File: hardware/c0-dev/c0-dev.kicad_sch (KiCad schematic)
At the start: 16 parts, among them J101 2913730000, J102 2913710000, J103 2913730000, J104 2913730000, J105 2913730000, J106 2913710000, J107 2913730000, J108 2913730000, J109 2913730000, J111 2913730000, J112 2913730000, J113 2913730000, J114 2913730000

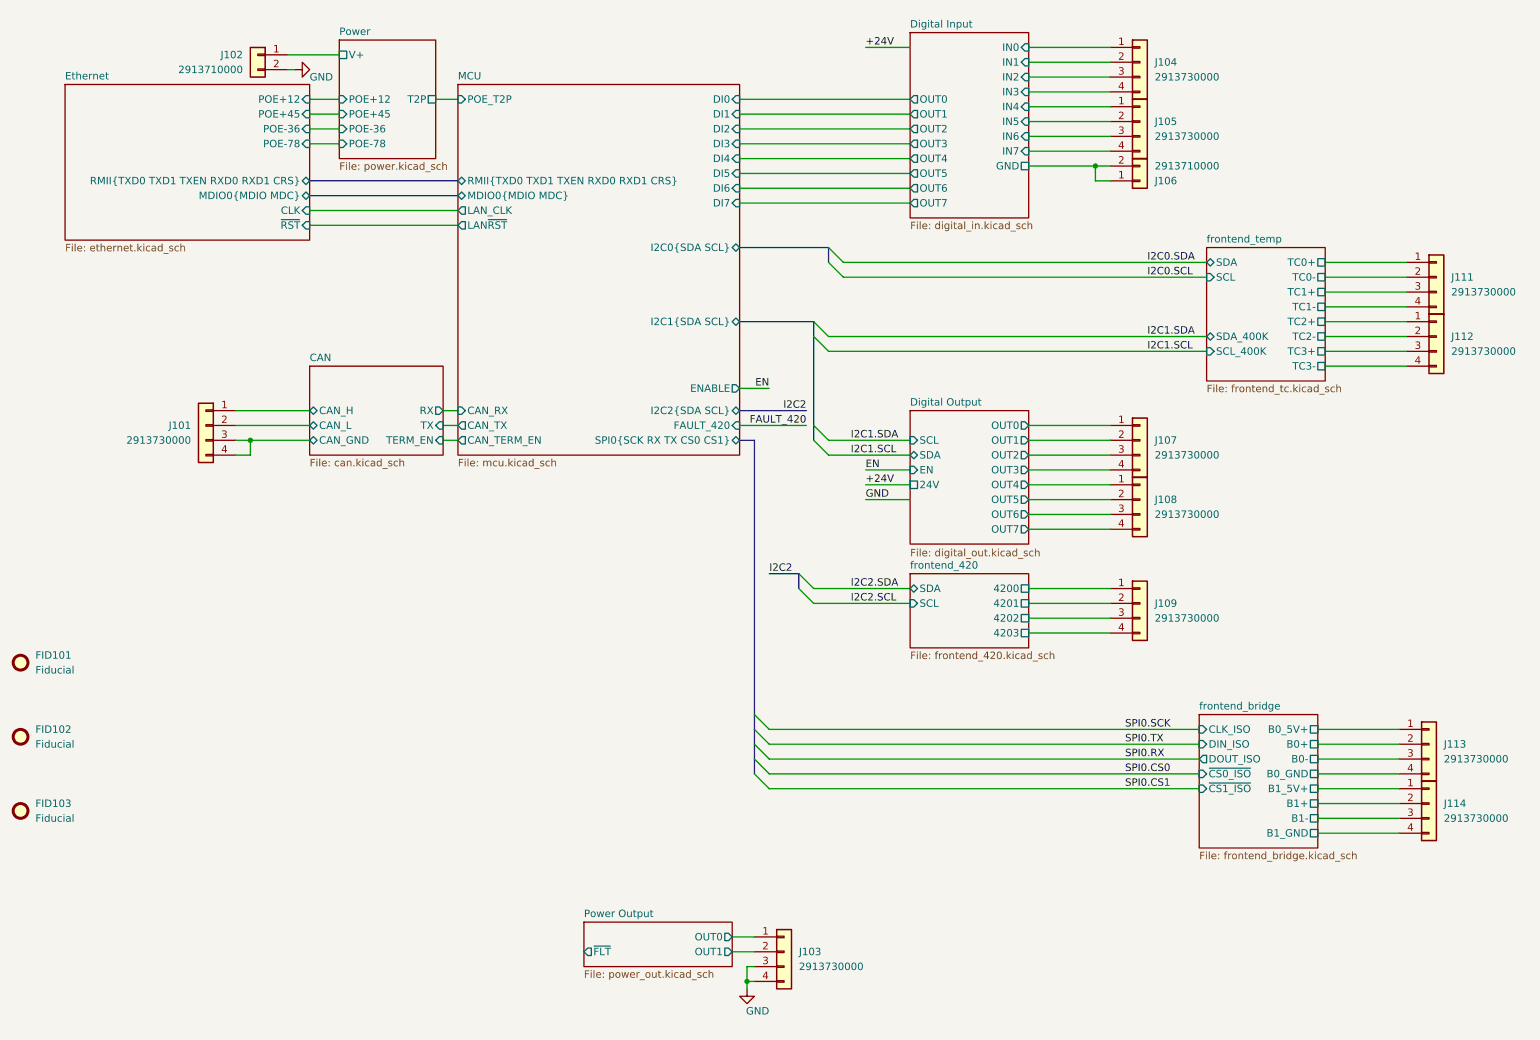
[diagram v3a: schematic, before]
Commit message: added LEDs
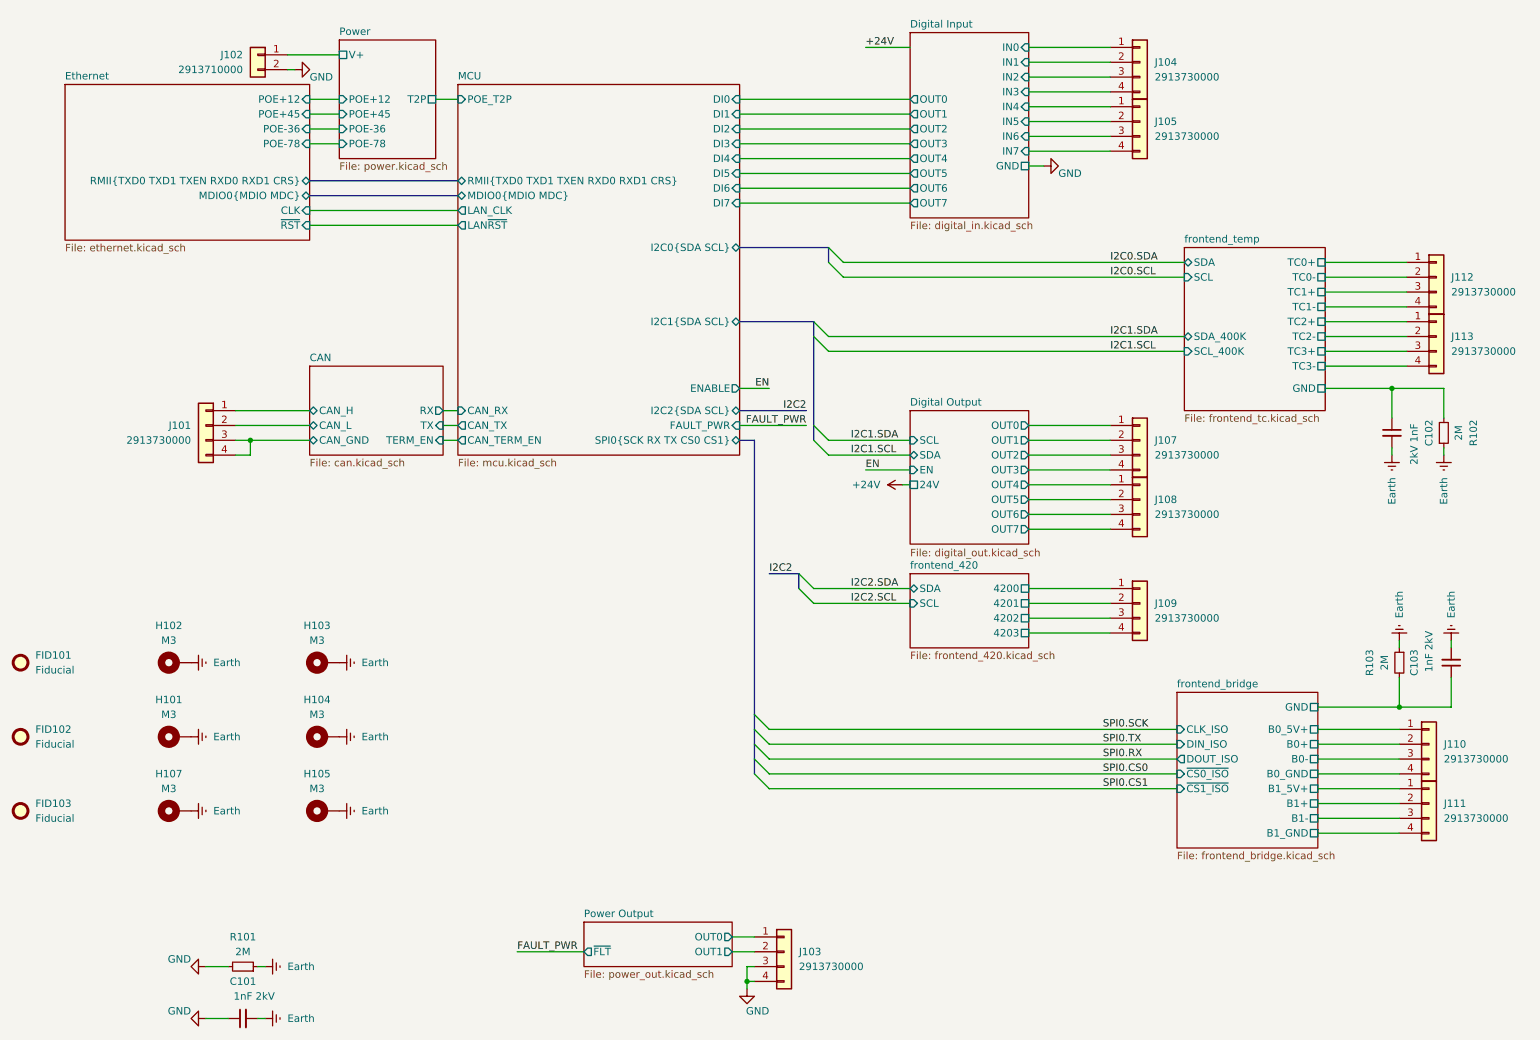
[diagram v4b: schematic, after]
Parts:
- removed J106: 2913710000, conduit:2913710000, symbol Connector_Generic:Conn_01x02
- added C101, C102, C103: 1nF, Capacitor_SMD:C_1206_3216Metric, symbol Device:C_Small
- added H101, H102, H103, H104, H105, H107: M3, MountingHole:MountingHole_3.5mm_Pad_TopBottom, symbol Mechanical:MountingHole_Pad
- added R101, R102, R103: 2M, Resistor_SMD:R_1206_3216Metric, symbol Device:R_Small
- renumbered J113 to J110, J114 to J111, J111 to J112, J112 to J113
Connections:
- net GND: now also C101.1, R101.2
- new net Earth: C101.2, C102.2, C103.2, H101.1, H102.1, H103.1, H104.1, H105.1, H107.1, R101.1, R102.1, R103.1
- new net frontend_bridge/GND: C103.1, R103.2
- new net frontend_temp/GND: C102.1, R102.2
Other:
- sheet MCU ports: added FAULT_PWR; removed FAULT_420
- sheet frontend_bridge ports: added GND; removed none
- sheet frontend_temp ports: added GND; removed none

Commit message: rgb's and 70x160mm
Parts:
- renumbered H102 to H101, H101 to H102, H107 to H103, H103 to H104, H104 to H105, H105 to H106, J107 to J106, J108 to J107, J109 to J108, J110 to J109, J111 to J110, J112 to J111, J113 to J112, R103 to R102, R102 to R103
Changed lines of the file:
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@@
 		(dnp no)
 		(fields_autoplaced yes)
-		(property "Reference" "H102"
+		(property "Reference" "H101"
 			(at 50.8 120.65 90)
 			(show_name no)
@@
 			(project "c0-dev"
 				(path "/b8347a0e-ad04-4414-969d-3c64a611d74e"
-					(reference "H102")
+					(reference "H101")
 					(unit 1)
 				)
@@
 		(dnp no)
 		(fields_autoplaced yes)
-		(property "Reference" "#PWR0109"
+		(property "Reference" "#PWR0117"
 			(at 269.24 97.79 0)
 			(hide yes)
@@
 			(project "c0-dev"
 				(path "/b8347a0e-ad04-4414-969d-3c64a611d74e"
-					(reference "#PWR0109")
+					(reference "#PWR0117")
 					(unit 1)
 				)
@@
 		(dnp no)
 		(fields_autoplaced yes)
-		(property "Reference" "#PWR0113"
+		(property "Reference" "#PWR0103"
 			(at 60.96 152.4 0)
 			(hide yes)
@@
 			(project "c0-dev"
 				(path "/b8347a0e-ad04-4414-969d-3c64a611d74e"
-					(reference "#PWR0113")
+					(reference "#PWR0103")
 					(unit 1)
 				)
@@
 		(dnp no)
 		(fields_autoplaced yes)
-		(property "Reference" "#PWR0115"
+		(property "Reference" "#PWR0101"
 			(at 60.96 127 0)
 			(hide yes)
@@
 			(project "c0-dev"
 				(path "/b8347a0e-ad04-4414-969d-3c64a611d74e"
-					(reference "#PWR0115")
+					(reference "#PWR0101")
 					(unit 1)
 				)
@@
 		(in_pos_files yes)
 		(dnp no)
-		(property "Reference" "R103"
+		(property "Reference" "R102"
 			(at 256.54 127 90)
 			(show_name no)
@@
 			(project "c0-dev"
 				(path "/b8347a0e-ad04-4414-969d-3c64a611d74e"
-					(reference "R103")
+					(reference "R102")
 					(unit 1)
 				)
@@
 		(dnp no)
 		(fields_autoplaced yes)
-		(property "Reference" "H101"
+		(property "Reference" "H102"
 			(at 50.8 133.35 90)
 			(show_name no)
@@
 			(project "c0-dev"
 				(path "/b8347a0e-ad04-4414-969d-3c64a611d74e"
-					(reference "H101")
+					(reference "H102")
 					(unit 1)
 				)
@@
 		(in_pos_files yes)
 		(dnp no)
-		(property "Reference" "R102"
+		(property "Reference" "R103"
 			(at 274.32 87.63 90)
 			(show_name no)
@@
 			(project "c0-dev"
 				(path "/b8347a0e-ad04-4414-969d-3c64a611d74e"
-					(reference "R102")
+					(reference "R103")
 					(unit 1)
 				)
@@
 		(dnp no)
 		(fields_autoplaced yes)
-		(property "Reference" "#PWR0108"
+		(property "Reference" "#PWR0113"
 			(at 180.34 96.52 0)
 			(hide yes)
@@
 			(project "c0-dev"
 				(path "/b8347a0e-ad04-4414-969d-3c64a611d74e"
-					(reference "#PWR0108")
+					(reference "#PWR0113")
 					(unit 1)
 				)
@@
 		(dnp no)
 		(fields_autoplaced yes)
-		(property "Reference" "#PWR0116"
+		(property "Reference" "#PWR0109"
 			(at 86.36 127 0)
 			(hide yes)
@@
 			(project "c0-dev"
 				(path "/b8347a0e-ad04-4414-969d-3c64a611d74e"
-					(reference "#PWR0116")
+					(reference "#PWR0109")
 					(unit 1)
 				)
@@
 		(dnp no)
 		(fields_autoplaced yes)
-		(property "Reference" "H105"
+		(property "Reference" "H106"
 			(at 76.2 146.05 90)
 			(show_name no)
@@
 			(project "c0-dev"
 				(path "/b8347a0e-ad04-4414-969d-3c64a611d74e"
-					(reference "H105")
+					(reference "H106")
 					(unit 1)
 				)
@@
 		(dnp no)
 		(fields_autoplaced yes)
-		(property "Reference" "J111"
+		(property "Reference" "J110"
 			(at 269.24 151.1299 0)
 			(show_name no)
@@
 			(project "c0-dev"
 				(path "/b8347a0e-ad04-4414-969d-3c64a611d74e"
-					(reference "J111")
+					(reference "J110")
 					(unit 1)
 				)
@@
 		(in_pos_files yes)
 		(dnp no)
-		(property "Reference" "#PWR0106"
+		(property "Reference" "#PWR0104"
 			(at 50.8 179.07 0)
 			(hide yes)
@@
 			(project "c0-dev"
 				(path "/b8347a0e-ad04-4414-969d-3c64a611d74e"
-					(reference "#PWR0106")
+					(reference "#PWR0104")
 					(unit 1)
 				)
@@
 		(dnp no)
 		(fields_autoplaced yes)
-		(property "Reference" "#PWR0114"
+		(property "Reference" "#PWR0102"
 			(at 60.96 139.7 0)
 			(hide yes)
@@
 			(project "c0-dev"
 				(path "/b8347a0e-ad04-4414-969d-3c64a611d74e"
-					(reference "#PWR0114")
+					(reference "#PWR0102")
 					(unit 1)
 				)
@@
 		(dnp no)
 		(fields_autoplaced yes)
-		(property "Reference" "J110"
+		(property "Reference" "J109"
 			(at 269.24 140.9699 0)
 			(show_name no)
@@
 			(project "c0-dev"
 				(path "/b8347a0e-ad04-4414-969d-3c64a611d74e"
-					(reference "J110")
+					(reference "J109")
 					(unit 1)
 				)
@@
 		(dnp no)
 		(fields_autoplaced yes)
-		(property "Reference" "H104"
+		(property "Reference" "H105"
 			(at 76.2 133.35 90)
 			(show_name no)
@@
 			(project "c0-dev"
 				(path "/b8347a0e-ad04-4414-969d-3c64a611d74e"
-					(reference "H104")
+					(reference "H105")
 					(unit 1)
 				)
@@
 		(dnp no)
 		(fields_autoplaced yes)
-		(property "Reference" "J109"
+		(property "Reference" "J108"
 			(at 219.71 116.8399 0)
 			(show_name no)
@@
 			(project "c0-dev"
 				(path "/b8347a0e-ad04-4414-969d-3c64a611d74e"
-					(reference "J109")
+					(reference "J108")
 					(unit 1)
 				)
@@
 		(dnp no)
 		(fields_autoplaced yes)
-		(property "Reference" "#PWR0118"
+		(property "Reference" "#PWR0111"
 			(at 86.36 152.4 0)
 			(hide yes)
@@
 			(project "c0-dev"
 				(path "/b8347a0e-ad04-4414-969d-3c64a611d74e"
-					(reference "#PWR0118")
+					(reference "#PWR0111")
 					(unit 1)
 				)
@@
 		(dnp no)
 		(fields_autoplaced yes)
-		(property "Reference" "#PWR0117"
+		(property "Reference" "#PWR0110"
 			(at 86.36 139.7 0)
 			(hide yes)
@@
 			(project "c0-dev"
 				(path "/b8347a0e-ad04-4414-969d-3c64a611d74e"
-					(reference "#PWR0117")
+					(reference "#PWR0110")
 					(unit 1)
 				)
@@
 		(dnp no)
 		(fields_autoplaced yes)
-		(property "Reference" "J112"
+		(property "Reference" "J111"
 			(at 270.51 60.9599 0)
 			(show_name no)
@@
 			(project "c0-dev"
 				(path "/b8347a0e-ad04-4414-969d-3c64a611d74e"
-					(reference "J112")
+					(reference "J111")
 					(unit 1)
 				)
@@
 		(dnp no)
 		(fields_autoplaced yes)
-		(property "Reference" "#PWR0111"
+		(property "Reference" "#PWR0118"
 			(at 270.51 116.84 0)
 			(hide yes)
@@
 			(project "c0-dev"
 				(path "/b8347a0e-ad04-4414-969d-3c64a611d74e"
-					(reference "#PWR0111")
+					(reference "#PWR0118")
 					(unit 1)
 				)
@@
 		(in_pos_files yes)
 		(dnp no)
-		(property "Reference" "#PWR0103"
+		(property "Reference" "#PWR0114"
 			(at 207.01 41.91 0)
 			(hide yes)
@@
 			(project "c0-dev"
 				(path "/b8347a0e-ad04-4414-969d-3c64a611d74e"
-					(reference "#PWR0103")
+					(reference "#PWR0114")
 					(unit 1)
 				)
@@
 		(dnp no)
 		(fields_autoplaced yes)
-		(property "Reference" "#PWR0105"
+		(property "Reference" "#PWR0107"
 			(at 73.66 187.96 0)
 			(hide yes)
@@
 			(project "c0-dev"
 				(path "/b8347a0e-ad04-4414-969d-3c64a611d74e"
-					(reference "#PWR0105")
+					(reference "#PWR0107")
 					(unit 1)
 				)
@@
 		(dnp no)
 		(fields_autoplaced yes)
-		(property "Reference" "H103"
+		(property "Reference" "H104"
 			(at 76.2 120.65 90)
 			(show_name no)
@@
 			(project "c0-dev"
 				(path "/b8347a0e-ad04-4414-969d-3c64a611d74e"
-					(reference "H103")
+					(reference "H104")
 					(unit 1)
 				)
@@
 		(dnp no)
 		(fields_autoplaced yes)
-		(property "Reference" "#PWR0110"
+		(property "Reference" "#PWR0115"
 			(at 260.35 97.79 0)
 			(hide yes)
@@
 			(project "c0-dev"
 				(path "/b8347a0e-ad04-4414-969d-3c64a611d74e"
-					(reference "#PWR0110")
+					(reference "#PWR0115")
 					(unit 1)
 				)
@@
 		(in_pos_files yes)
 		(dnp no)
-		(property "Reference" "#PWR0102"
+		(property "Reference" "#PWR0112"
 			(at 149.86 189.23 0)
 			(hide yes)
@@
 			(project "c0-dev"
 				(path "/b8347a0e-ad04-4414-969d-3c64a611d74e"
-					(reference "#PWR0102")
+					(reference "#PWR0112")
 					(unit 1)
 				)
@@
 		(dnp no)
 		(fields_autoplaced yes)
-		(property "Reference" "H107"
+		(property "Reference" "H103"
 			(at 50.8 146.05 90)
 			(show_name no)
@@
 			(project "c0-dev"
 				(path "/b8347a0e-ad04-4414-969d-3c64a611d74e"
-					(reference "H107")
+					(reference "H103")
 					(unit 1)
 				)
@@
 		(in_pos_files yes)
 		(dnp no)
-		(property "Reference" "#PWR0101"
+		(property "Reference" "#PWR0108"
 			(at 78.74 25.4 0)
 			(hide yes)
@@
 			(project "c0-dev"
 				(path "/b8347a0e-ad04-4414-969d-3c64a611d74e"
-					(reference "#PWR0101")
+					(reference "#PWR0108")
 					(unit 1)
 				)
@@
 		(dnp no)
 		(fields_autoplaced yes)
-		(property "Reference" "#PWR0112"
+		(property "Reference" "#PWR0116"
 			(at 261.62 116.84 0)
 			(hide yes)
@@
 			(project "c0-dev"
 				(path "/b8347a0e-ad04-4414-969d-3c64a611d74e"
-					(reference "#PWR0112")
+					(reference "#PWR0116")
 					(unit 1)
 				)
@@
 		(in_pos_files yes)
 		(dnp no)
-		(property "Reference" "#PWR0107"
+		(property "Reference" "#PWR0105"
 			(at 50.8 187.96 0)
 			(hide yes)
@@
 			(project "c0-dev"
 				(path "/b8347a0e-ad04-4414-969d-3c64a611d74e"
-					(reference "#PWR0107")
+					(reference "#PWR0105")
 					(unit 1)
 				)
@@
 		(dnp no)
 		(fields_autoplaced yes)
-		(property "Reference" "J107"
+		(property "Reference" "J106"
 			(at 219.71 88.8999 0)
 			(show_name no)
@@
 			(project "c0-dev"
 				(path "/b8347a0e-ad04-4414-969d-3c64a611d74e"
-					(reference "J107")
+					(reference "J106")
 					(unit 1)
 				)
@@
 		(dnp no)
 		(fields_autoplaced yes)
-		(property "Reference" "#PWR0104"
+		(property "Reference" "#PWR0106"
 			(at 73.66 179.07 0)
 			(hide yes)
@@
 			(project "c0-dev"
 				(path "/b8347a0e-ad04-4414-969d-3c64a611d74e"
-					(reference "#PWR0104")
+					(reference "#PWR0106")
 					(unit 1)
 				)
@@
 		(dnp no)
 		(fields_autoplaced yes)
-		(property "Reference" "J113"
+		(property "Reference" "J112"
 			(at 270.51 71.1199 0)
 			(show_name no)
@@
 			(project "c0-dev"
 				(path "/b8347a0e-ad04-4414-969d-3c64a611d74e"
-					(reference "J113")
+					(reference "J112")
 					(unit 1)
 				)
@@
 		(dnp no)
 		(fields_autoplaced yes)
-		(property "Reference" "J108"
+		(property "Reference" "J107"
 			(at 219.71 99.0599 0)
 			(show_name no)
@@
 			(project "c0-dev"
 				(path "/b8347a0e-ad04-4414-969d-3c64a611d74e"
-					(reference "J108")
+					(reference "J107")
 					(unit 1)
 				)

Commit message: started PCB
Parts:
- removed J102: 2913710000, conduit:2913710000, symbol Connector_Generic:Conn_01x02
- added J102: 2913730000, conduit:2913730000, symbol Connector_Generic:Conn_01x04
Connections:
- net GND: now also J102.3 (Pin_3), J102.4 (Pin_4)
- net Power/V+: now also J102.1 (Pin_1), J102.2 (Pin_2)
- net frontend_bridge/GND renamed frontend_bridge/GND_BR
- net frontend_temp/GND renamed frontend_temp/GND_TC
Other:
- sheet CAN ports: added +3.3V_IN, +5V_IN, GND_IN; removed none
- sheet frontend_bridge ports: added +3.3V_IN, +5V_IN, GND_BR, GND_IN; removed GND
- sheet frontend_temp ports: added +3.3V_IN, +5V_IN, GND_IN, GND_TC; removed GND
- moved on the sheet: J106, J107, J108
